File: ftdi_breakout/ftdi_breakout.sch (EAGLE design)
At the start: 16 parts, among them U1 FT231XS

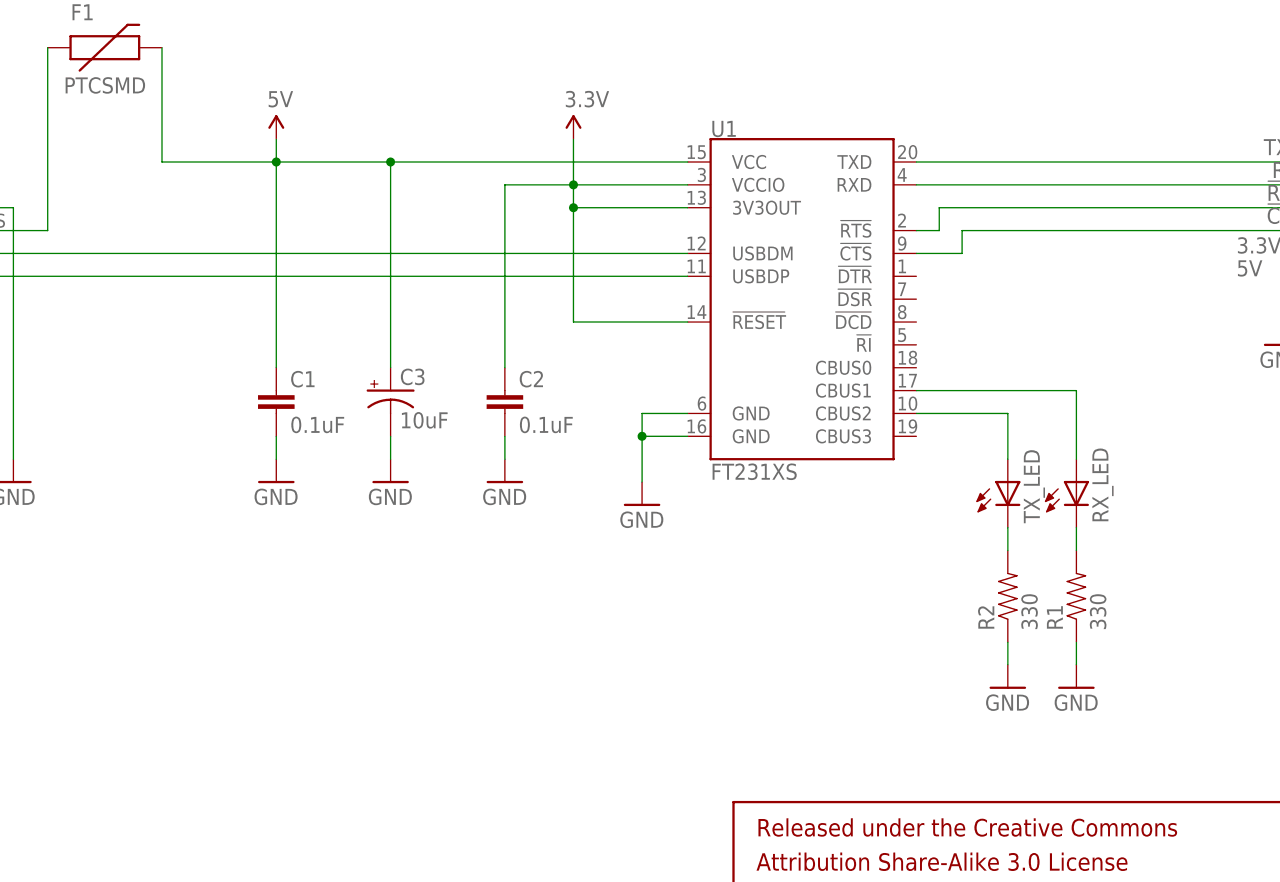
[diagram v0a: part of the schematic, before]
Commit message: Modified to connect the chip as sinking the current from LED.
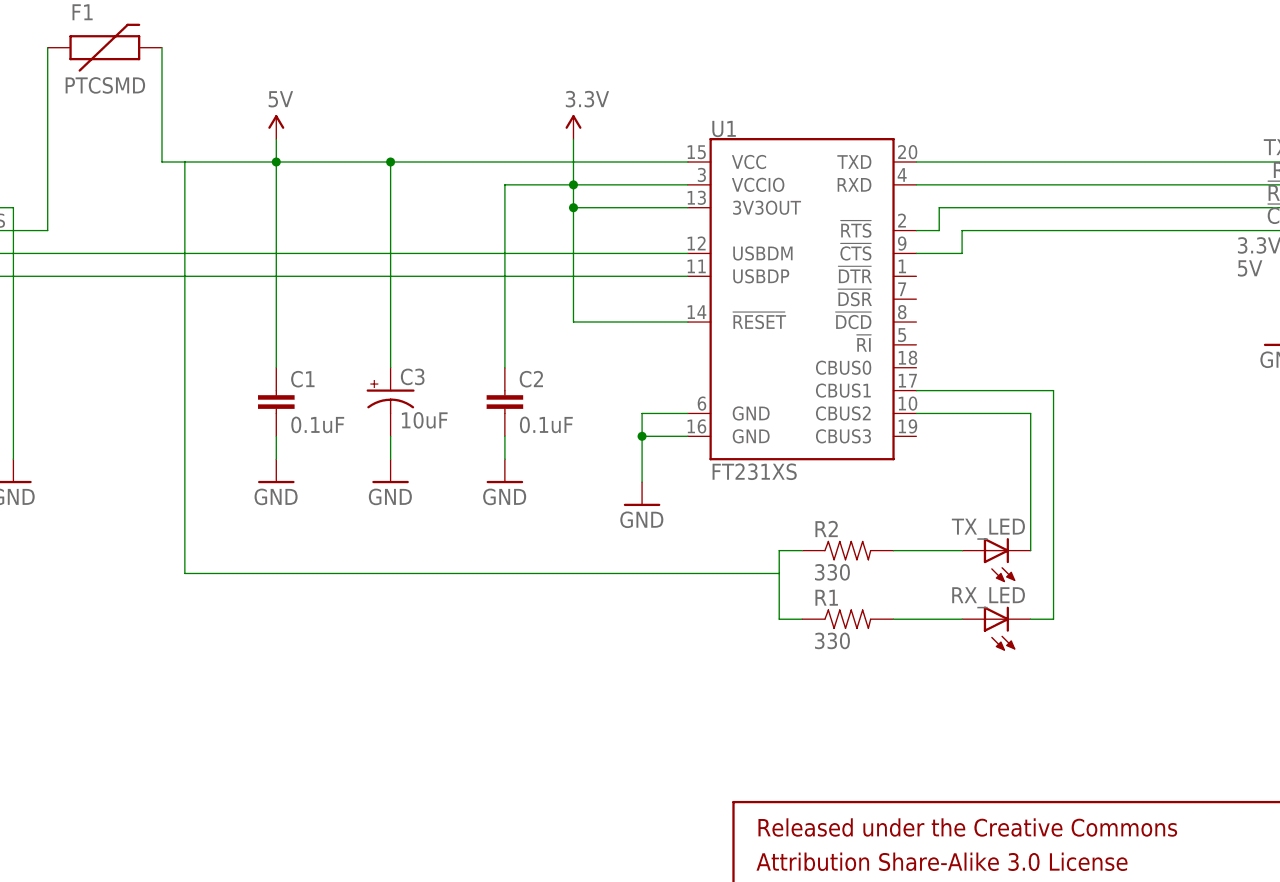
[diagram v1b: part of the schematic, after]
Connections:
- net 5V: now also R1.1, R2.1
- net GND: no longer R1.1, R2.1
- net N$4: now also RX_LED.C; no longer RX_LED.A
- net N$5: now also TX_LED.C; no longer TX_LED.A
- net N$6: now also TX_LED.A; no longer TX_LED.C
- net N$7: now also RX_LED.A; no longer RX_LED.C
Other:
- moved on the sheet: R1, R2, RX_LED, TX_LED
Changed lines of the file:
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@@
 <part name="SUPPLY1" library="SparkFun-Aesthetics" deviceset="5V" device=""/>
 <part name="SUPPLY2" library="SparkFun-Aesthetics" deviceset="3.3V" device=""/>
-<part name="GND1" library="SparkFun-Aesthetics" deviceset="GND" device=""/>
 <part name="RX_LED" library="SparkFun-LED" deviceset="LED" device="0603"/>
 <part name="TX_LED" library="SparkFun-LED" deviceset="LED" device="0603"/>
@@
 <part name="STANDOFF3" library="SparkFun-Electromechanical" deviceset="STAND-OFF" device=""/>
 <part name="STANDOFF4" library="SparkFun-Electromechanical" deviceset="STAND-OFF" device=""/>
-<part name="GND2" library="SparkFun-Aesthetics" deviceset="GND" device=""/>
 <part name="GND3" library="SparkFun-Aesthetics" deviceset="GND" device=""/>
 <part name="GND4" library="SparkFun-Aesthetics" deviceset="GND" device=""/>
@@
 <instance part="SUPPLY1" gate="G$1" x="96.52" y="111.76"/>
 <instance part="SUPPLY2" gate="G$1" x="129.54" y="111.76"/>
-<instance part="GND1" gate="1" x="177.8" y="50.8"/>
-<instance part="RX_LED" gate="G$1" x="185.42" y="73.66"/>
-<instance part="TX_LED" gate="G$1" x="177.8" y="73.66"/>
+<instance part="RX_LED" gate="G$1" x="175.26" y="58.42" rot="R90"/>
+<instance part="TX_LED" gate="G$1" x="175.26" y="66.04" rot="R90"/>
 <instance part="C1" gate="G$1" x="96.52" y="81.28"/>
 <instance part="C2" gate="G$1" x="121.92" y="81.28"/>
 <instance part="C3" gate="G$1" x="109.22" y="83.82"/>
-<instance part="R1" gate="G$1" x="185.42" y="60.96" rot="R90"/>
-<instance part="R2" gate="G$1" x="177.8" y="60.96" rot="R90"/>
+<instance part="R1" gate="G$1" x="160.02" y="58.42"/>
+<instance part="R2" gate="G$1" x="160.02" y="66.04"/>
 <instance part="F1" gate="G$1" x="76.2" y="121.92"/>
 <instance part="STANDOFF1" gate="G$1" x="17.78" y="20.32"/>
@@
 <instance part="STANDOFF3" gate="G$1" x="17.78" y="15.24"/>
 <instance part="STANDOFF4" gate="G$1" x="27.94" y="15.24"/>
-<instance part="GND2" gate="1" x="185.42" y="50.8"/>
 <instance part="GND3" gate="1" x="96.52" y="73.66"/>
 <instance part="GND4" gate="1" x="109.22" y="73.66"/>
@@
 <wire x1="83.82" y1="121.92" x2="83.82" y2="109.22" width="0.1524" layer="91"/>
 <pinref part="U1" gate="G$1" pin="VCC"/>
-<wire x1="83.82" y1="109.22" x2="96.52" y2="109.22" width="0.1524" layer="91"/>
+<wire x1="83.82" y1="109.22" x2="86.36" y2="109.22" width="0.1524" layer="91"/>
+<wire x1="86.36" y1="109.22" x2="96.52" y2="109.22" width="0.1524" layer="91"/>
 <wire x1="96.52" y1="109.22" x2="109.22" y2="109.22" width="0.1524" layer="91"/>
 <wire x1="109.22" y1="109.22" x2="142.24" y2="109.22" width="0.1524" layer="91"/>
@@
 <junction x="96.52" y="109.22"/>
 <junction x="109.22" y="109.22"/>
+<pinref part="R2" gate="G$1" pin="1"/>
+<wire x1="154.94" y1="66.04" x2="152.4" y2="66.04" width="0.1524" layer="91"/>
+<pinref part="R1" gate="G$1" pin="1"/>
+<wire x1="154.94" y1="58.42" x2="152.4" y2="58.42" width="0.1524" layer="91"/>
+<wire x1="152.4" y1="58.42" x2="152.4" y2="63.5" width="0.1524" layer="91"/>
+<wire x1="152.4" y1="63.5" x2="152.4" y2="66.04" width="0.1524" layer="91"/>
+<wire x1="152.4" y1="63.5" x2="86.36" y2="63.5" width="0.1524" layer="91"/>
+<wire x1="86.36" y1="63.5" x2="86.36" y2="109.22" width="0.1524" layer="91"/>
 </segment>
 <segment>
@@
 </segment>
 </net>
-<net name="N$6" class="0">
-<segment>
-<pinref part="TX_LED" gate="G$1" pin="C"/>
-<pinref part="R2" gate="G$1" pin="2"/>
-<wire x1="177.8" y1="68.58" x2="177.8" y2="66.04" width="0.1524" layer="91"/>
-</segment>
-</net>
-<net name="N$7" class="0">
-<segment>
-<pinref part="RX_LED" gate="G$1" pin="C"/>
-<pinref part="R1" gate="G$1" pin="2"/>
-<wire x1="185.42" y1="68.58" x2="185.42" y2="66.04" width="0.1524" layer="91"/>
-</segment>
-</net>
 <net name="GND" class="0">
 <segment>
@@
 </segment>
 <segment>
-<pinref part="R2" gate="G$1" pin="1"/>
-<pinref part="GND1" gate="1" pin="GND"/>
-<wire x1="177.8" y1="55.88" x2="177.8" y2="53.34" width="0.1524" layer="91"/>
-</segment>
-<segment>
-<pinref part="R1" gate="G$1" pin="1"/>
-<pinref part="GND2" gate="1" pin="GND"/>
-<wire x1="185.42" y1="55.88" x2="185.42" y2="53.34" width="0.1524" layer="91"/>
-</segment>
-<segment>
 <pinref part="JP1" gate="G$1" pin="7"/>
 <wire x1="210.82" y1="93.98" x2="208.28" y2="93.98" width="0.1524" layer="91"/>
@@
 <segment>
 <pinref part="U1" gate="G$1" pin="CBUS2"/>
-<wire x1="167.64" y1="81.28" x2="177.8" y2="81.28" width="0.1524" layer="91"/>
-<pinref part="TX_LED" gate="G$1" pin="A"/>
-<wire x1="177.8" y1="81.28" x2="177.8" y2="76.2" width="0.1524" layer="91"/>
+<wire x1="167.64" y1="81.28" x2="180.34" y2="81.28" width="0.1524" layer="91"/>
+<pinref part="TX_LED" gate="G$1" pin="C"/>
+<wire x1="180.34" y1="81.28" x2="180.34" y2="66.04" width="0.1524" layer="91"/>
 </segment>
 </net>
@@
 <segment>
 <pinref part="U1" gate="G$1" pin="CBUS1"/>
-<wire x1="167.64" y1="83.82" x2="185.42" y2="83.82" width="0.1524" layer="91"/>
-<pinref part="RX_LED" gate="G$1" pin="A"/>
-<wire x1="185.42" y1="83.82" x2="185.42" y2="76.2" width="0.1524" layer="91"/>
+<wire x1="167.64" y1="83.82" x2="182.88" y2="83.82" width="0.1524" layer="91"/>
+<pinref part="RX_LED" gate="G$1" pin="C"/>
+<wire x1="180.34" y1="58.42" x2="182.88" y2="58.42" width="0.1524" layer="91"/>
+<wire x1="182.88" y1="58.42" x2="182.88" y2="83.82" width="0.1524" layer="91"/>
 </segment>
 </net>
@@
 </segment>
 </net>
+<net name="N$6" class="0">
+<segment>
+<pinref part="R2" gate="G$1" pin="2"/>
+<pinref part="TX_LED" gate="G$1" pin="A"/>
+<wire x1="165.1" y1="66.04" x2="172.72" y2="66.04" width="0.1524" layer="91"/>
+</segment>
+</net>
+<net name="N$7" class="0">
+<segment>
+<pinref part="R1" gate="G$1" pin="2"/>
+<pinref part="RX_LED" gate="G$1" pin="A"/>
+<wire x1="165.1" y1="58.42" x2="172.72" y2="58.42" width="0.1524" layer="91"/>
+</segment>
+</net>
